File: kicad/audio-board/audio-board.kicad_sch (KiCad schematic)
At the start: 23 parts, among them U1 ADAU1861, U2 ADXL354CEZ, U3 LTC6242

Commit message: [LIMA] add IM72D128V PDM DMIC to the audio board - wired into U1's DMIC01/DMIC_CLK per docs/sensor-head-design-note.md S8
New Infineon.kicad_sym with the IM72D128V symbol (pinout from docs/datasheets/IM72D128V_v01_00.pdf
Table 9). Digital-only per the design note: no coupling, no buffer - straight into ADAU1861's
DMIC01/MP1 and DMIC_CLK/MP0. VDD on 1V8 (not 3V3, per JULIETT's 2026-09-17-004) with a 1uF bypass
cap at the VDD pad per the datasheet's footnote 3. LR tied to AGND (DATA1 channel) - my choice, not
specified anywhere, flagged in the schematic's open-items note for DSP-side confirmation. DMIC23/MP2
(the second mic pair) marked no-connect since this board carries one mic.
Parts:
- added C18: 1uF, symbol Device:C
- added U4: IM72D128VV01, symbol Infineon:IM72D128V
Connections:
- net 1V8: now also C18.1, U4.2 (VDD)
- net AGND: now also C18.2, U4.4 (LR), U4.5 (GND)
- net DMIC_DATA: now reaches U1.1 (DMIC01/MP1)
- net DMIC_DATA: now also U4.1 (DATA)
- net DMIC_CLK: now reaches U1.7 (DMIC_CLK/MP0)
- net DMIC_CLK: now also U4.3 (CLOCK)
- no-connect marks 13 -> 14
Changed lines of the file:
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@@
 		(at 72.39 86.36)
+	)
+	(no_connect
+		(at 234.95 142.24)
 	)
 	(wire
@@
 		)
 	)
-  (text "PRELIM - ADXL354 single-ended front end into the ADAU1861.\nPer docs/sensor-head-design-note.md and\ndocs/audio-board-decision-record.md (Decision B: ADAU1861\nruled, ADAU1372 rejected for this board).\n\nWIRED: ADAU1861 full power tree (1V8/AGND) + boot straps\n(PD, SELFBOOT, ROM_BOOT_MODE, REG_EN - tied to safe\ndefaults, [assumed], not checked against UG-2257's boot\nsection yet). ADXL354 X/Y/Z -> 100nF C0G coupling ->\n1Mohm bias to buffered CM -> LTC6242 unity-gain buffers\n-> AINN0/1/2, single-ended (AINP0/1/2 tied to raw CM).\n4th LTC6242 unit buffers CM per design note S6.\n\nNOT WIRED (deliberately, out of scope this pass):\ncontrol port (I2C/SPI), SAP0/SAP1 digital audio, JTAG,\nDMIC, UART, IRQ, QSPIM self-boot flash, headphone/line\noutputs, XTAL. ERC's 35 \"not connected\" errors are\nexactly these pins - expected, not a defect.\n\nOPEN ITEMS (design note S10 + new): buffer-to-AINNx\ncoupling (DC direct vs. footprint a series cap + 0R\njumper) not resolved here. CM pin loading not measured.\nSupply rail \"3V3_ACCEL\" is my judgment call, not in the\nnote - confirm before layout. REG_EN tied low assumes\nDVDD is externally supplied on 1V8, not the internal\nregulator - reasoned, not confirmed against the\ndatasheet's regulator sequencing section."
+	(label "1V8"
+		(at 177.8 121.92 0)
+		(effects
+			(font
+				(size 1.27 1.27)
+			)
+			(justify left bottom)
+		)
+	)
+	(label "AGND"
+		(at 177.8 129.54 0)
+		(effects
+			(font
+				(size 1.27 1.27)
+			)
+			(justify left bottom)
+		)
+	)
+	(label "DMIC_DATA"
+		(at 165.1 146.05 180)
+		(effects
+			(font
+				(size 1.27 1.27)
+			)
+			(justify right bottom)
+		)
+	)
+	(label "DMIC_CLK"
+		(at 190.5 146.05 0)
+		(effects
+			(font
+				(size 1.27 1.27)
+			)
+			(justify left bottom)
+		)
+	)
+	(label "AGND"
+		(at 190.5 148.59 0)
+		(effects
+			(font
+				(size 1.27 1.27)
+			)
+			(justify left bottom)
+		)
+	)
+	(label "1V8"
+		(at 177.8 160.02 0)
+		(effects
+			(font
+				(size 1.27 1.27)
+			)
+			(justify left bottom)
+		)
+	)
+	(label "AGND"
+		(at 177.8 134.62 0)
+		(effects
+			(font
+				(size 1.27 1.27)
+			)
+			(justify left bottom)
+		)
+	)
+	(label "DMIC_DATA"
+		(at 234.95 139.7 180)
+		(effects
+			(font
+				(size 1.27 1.27)
+			)
+			(justify right bottom)
+		)
+	)
+	(label "DMIC_CLK"
+		(at 234.95 144.78 180)
+		(effects
+			(font
+				(size 1.27 1.27)
+			)
+			(justify right bottom)
+		)
+	)
+  (text "PRELIM - ADXL354 single-ended front end into the ADAU1861.\nPer docs/sensor-head-design-note.md and\ndocs/audio-board-decision-record.md (Decision B: ADAU1861\nruled, ADAU1372 rejected for this board).\n\nWIRED: ADAU1861 full power tree (1V8/AGND) + boot straps\n(PD, SELFBOOT, ROM_BOOT_MODE, REG_EN - tied to safe\ndefaults, [assumed], not checked against UG-2257's boot\nsection yet). ADXL354 X/Y/Z -> 100nF C0G coupling ->\n1Mohm bias to buffered CM -> LTC6242 unity-gain buffers\n-> AINN0/1/2, single-ended (AINP0/1/2 tied to raw CM).\n4th LTC6242 unit buffers CM per design note S6.\nIM72D128V PDM mic -> DMIC01/DMIC_CLK on U1, per design\nnote S8 (digital-only, no coupling/buffer). VDD on 1V8\nwith 1uF bypass per datasheet footnote 3; LR tied to\nAGND (DATA1 channel). DMIC23/MP2 (2nd mic pair) marked\nno-connect - this board carries one mic.\n\nNOT WIRED (deliberately, out of scope this pass):\ncontrol port (I2C/SPI), SAP0/SAP1 digital audio, JTAG,\nUART, IRQ, QSPIM self-boot flash, headphone/line\noutputs, XTAL. ERC's \"not connected\" errors are exactly\nthese pins - expected, not a defect.\n\nOPEN ITEMS (design note S10 + new): buffer-to-AINNx\ncoupling (DC direct vs. footprint a series cap + 0R\njumper) not resolved here. CM pin loading not measured.\nSupply rail \"3V3_ACCEL\" is my judgment call, not in the\nnote - confirm before layout. REG_EN tied low assumes\nDVDD is externally supplied on 1V8, not the internal\nregulator - reasoned, not confirmed against the\ndatasheet's regulator sequencing section. DMIC LR=GND\n(DATA1) is my channel choice, not specified anywhere -\nconfirm against however the DSP expects the PDM stream\nframed."
     (at 100 215 0)
     (effects (font (size 1.2 1.2)))
@@
 					(unit 1)
 				)
+			)
+		)
+	)
+	(symbol
+		(lib_id "Infineon:IM72D128V")
+		(at 177.8 147.32 0)
+		(unit 1)
+		(in_bom yes)
+		(on_board yes)
+		(dnp no)
+		(property "Reference" "U4"
+			(at 177.8 134.62 0)
+			(effects
+				(font
+					(size 1.27 1.27)
+				)
+			)
+		)
+		(property "Value" "IM72D128VV01"
+			(at 177.8 160.02 0)
+			(effects
+				(font
+					(size 1.27 1.27)
+				)
+			)
+		)
+		(property "Footprint" ""
+			(at 177.8 147.32 0)
+			(hide yes)
+			(effects
+				(font
+					(size 1.27 1.27)
+				)
+			)
+		)
+		(property "Datasheet" "${KIPRJMOD}/../../docs/datasheets/IM72D128V_v01_00.pdf"
+			(at 177.8 147.32 0)
+			(hide yes)
+			(effects
+				(font
+					(size 1.27 1.27)
+				)
+			)
+		)
+		(instances
+			(project "audio-board"
+				(path "/58a3c587-b916-49c7-924f-a7f93d6c8ece"
+					(reference "U4")
+					(unit 1)
+				)
+			)
+		)
+	)
+	(symbol
+		(lib_id "Device:C")
+		(at 177.8 125.73 0)
+		(unit 1)
+		(in_bom yes)
+		(on_board yes)
+		(dnp no)
+		(property "Reference" "C18"
+			(at 178.435 123.19 0)
+			(effects
+				(font
+					(size 1.27 1.27)
+				)
+				(justify left)
+			)
+		)
+		(property "Value" "1uF"
+			(at 178.435 128.27 0)
+			(effects
+				(font
+					(size 1.27 1.27)
+				)
+				(justify left)
+			)
+		)
+		(property "Footprint" ""
+			(at 177.8 125.73 0)
+			(hide yes)
+			(effects
+				(font
+					(size 1.27 1.27)
+				)
+			)
+		)
+		(property "Datasheet" ""
+			(at 177.8 125.73 0)
+			(hide yes)
+			(effects
+				(font
+					(size 1.27 1.27)
+				)
+			)
+		)
+		(instances
+			(project "audio-board"
+				(path "/58a3c587-b916-49c7-924f-a7f93d6c8ece"
+					(reference "C18")
+					(unit 1)
+				)

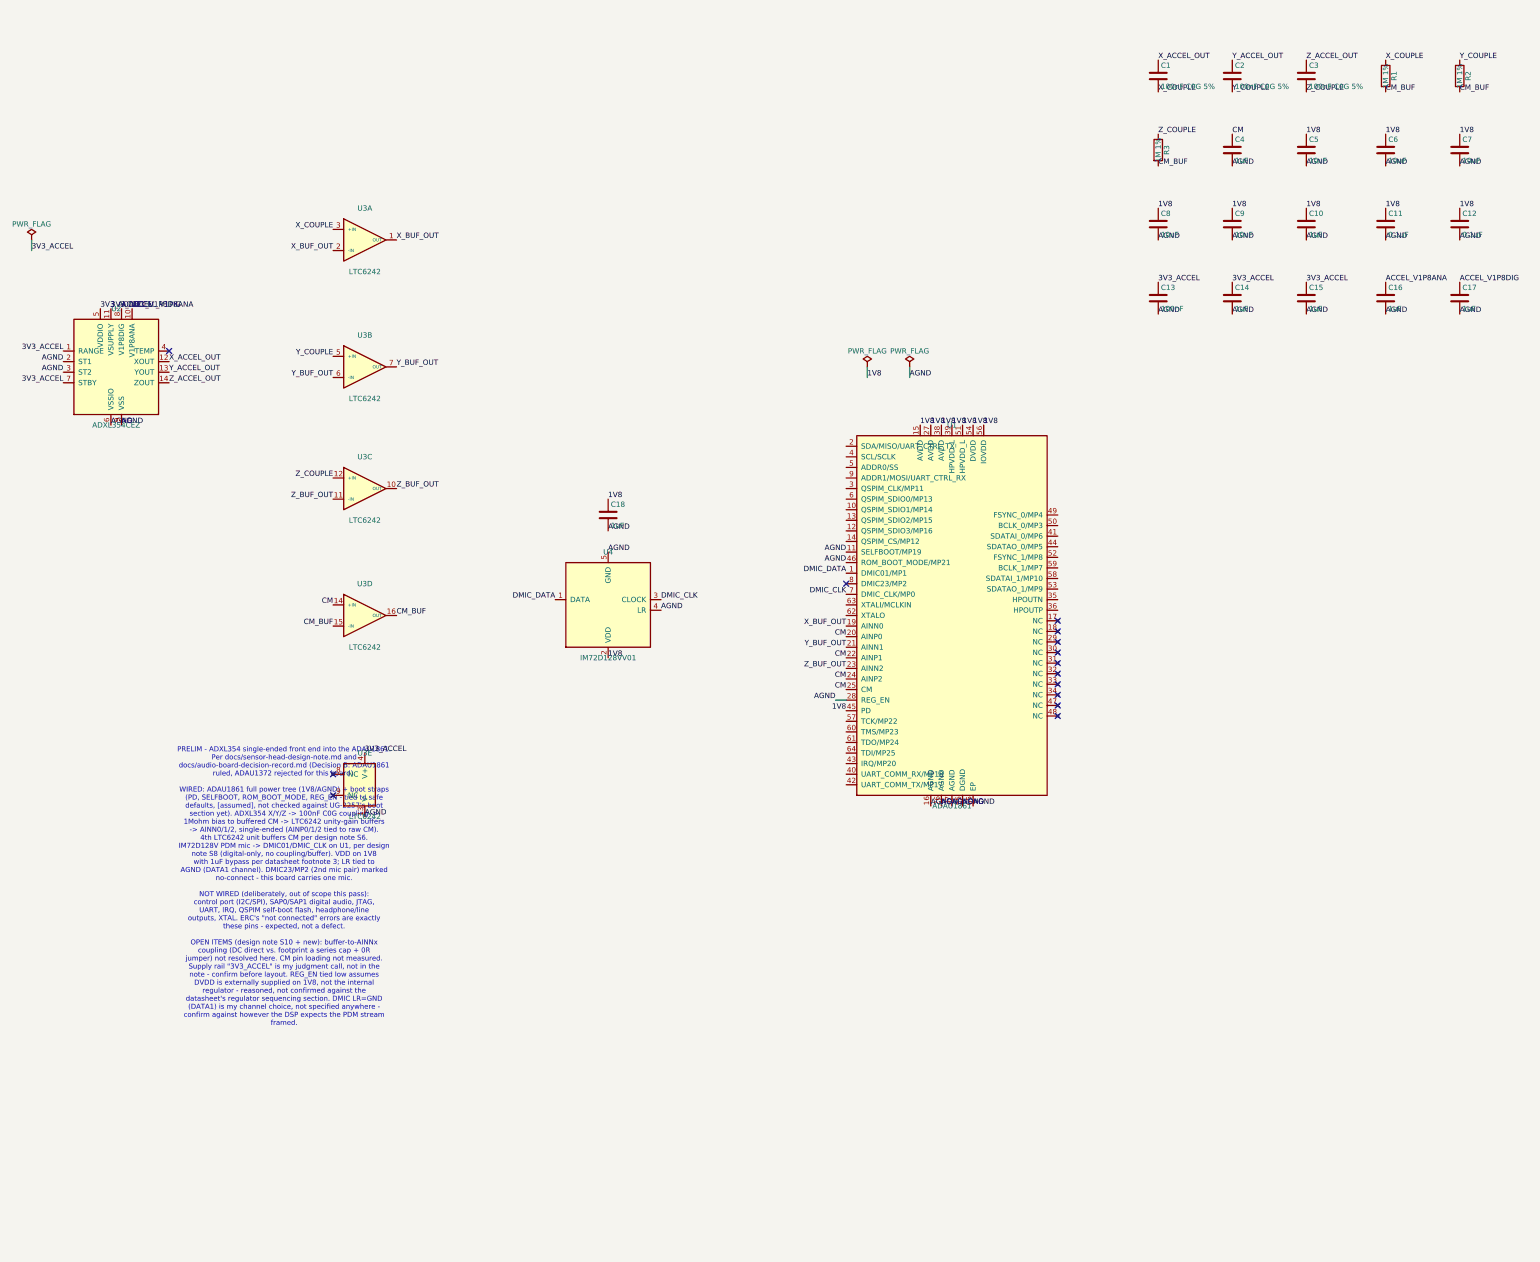
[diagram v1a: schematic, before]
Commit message: [LIMA] place AD2428 A2B transceiver on the audio board - host-side master node, for future connection to the earcups
New AD2428 symbol in AnalogDevices.kicad_sym (32-lead LFCSP_SS + EPAD, pinout from Table 15 of
docs/datasheets/AD242x_RevC.pdf). Per docs/audio-board-decision-record.md Decision C, this board's
AD2428 is the A2B bus MASTER: RP1 drives its I2S/TDM interface, and its Transceiver B pair runs
downstream to the per-cup slave transceivers.

Only wired what's unambiguous and chip-intrinsic: the on-chip LDO network (VOUT1 -> DVDD/PLLVDD,
VOUT2 -> ATRXVDD/BTRXVDD) with the datasheet's own decoupling values (4.7uF on each VOUTx, shared
100nF+10nF on the TRXVDD pins), and VSS/EPAD -> AGND (EPAD-to-GND is mandatory per the datasheet, not
a choice). Deliberately left open, flagged in the schematic's own note rather than guessed: VIN
(needs 3.7-9.0V, no such rail exists on this board yet), IOVDD's voltage domain (3.3V vs 1.8V,
decides whether U5 needs the same translators as the 1861), the entire host I2S/TDM + I2C interface,
the A2B bus-coupling network (the datasheet defers this to "contact your local ADI rep," which
docs/audio-board-decision-record.md's open item on the EVAL-AD2428WG1BZ already anticipated), and
whether the cups are bus-powered (decides SWP/VSSN/SENSE). ERC clean on everything wired; every new
"not connected" is one of these named opens.
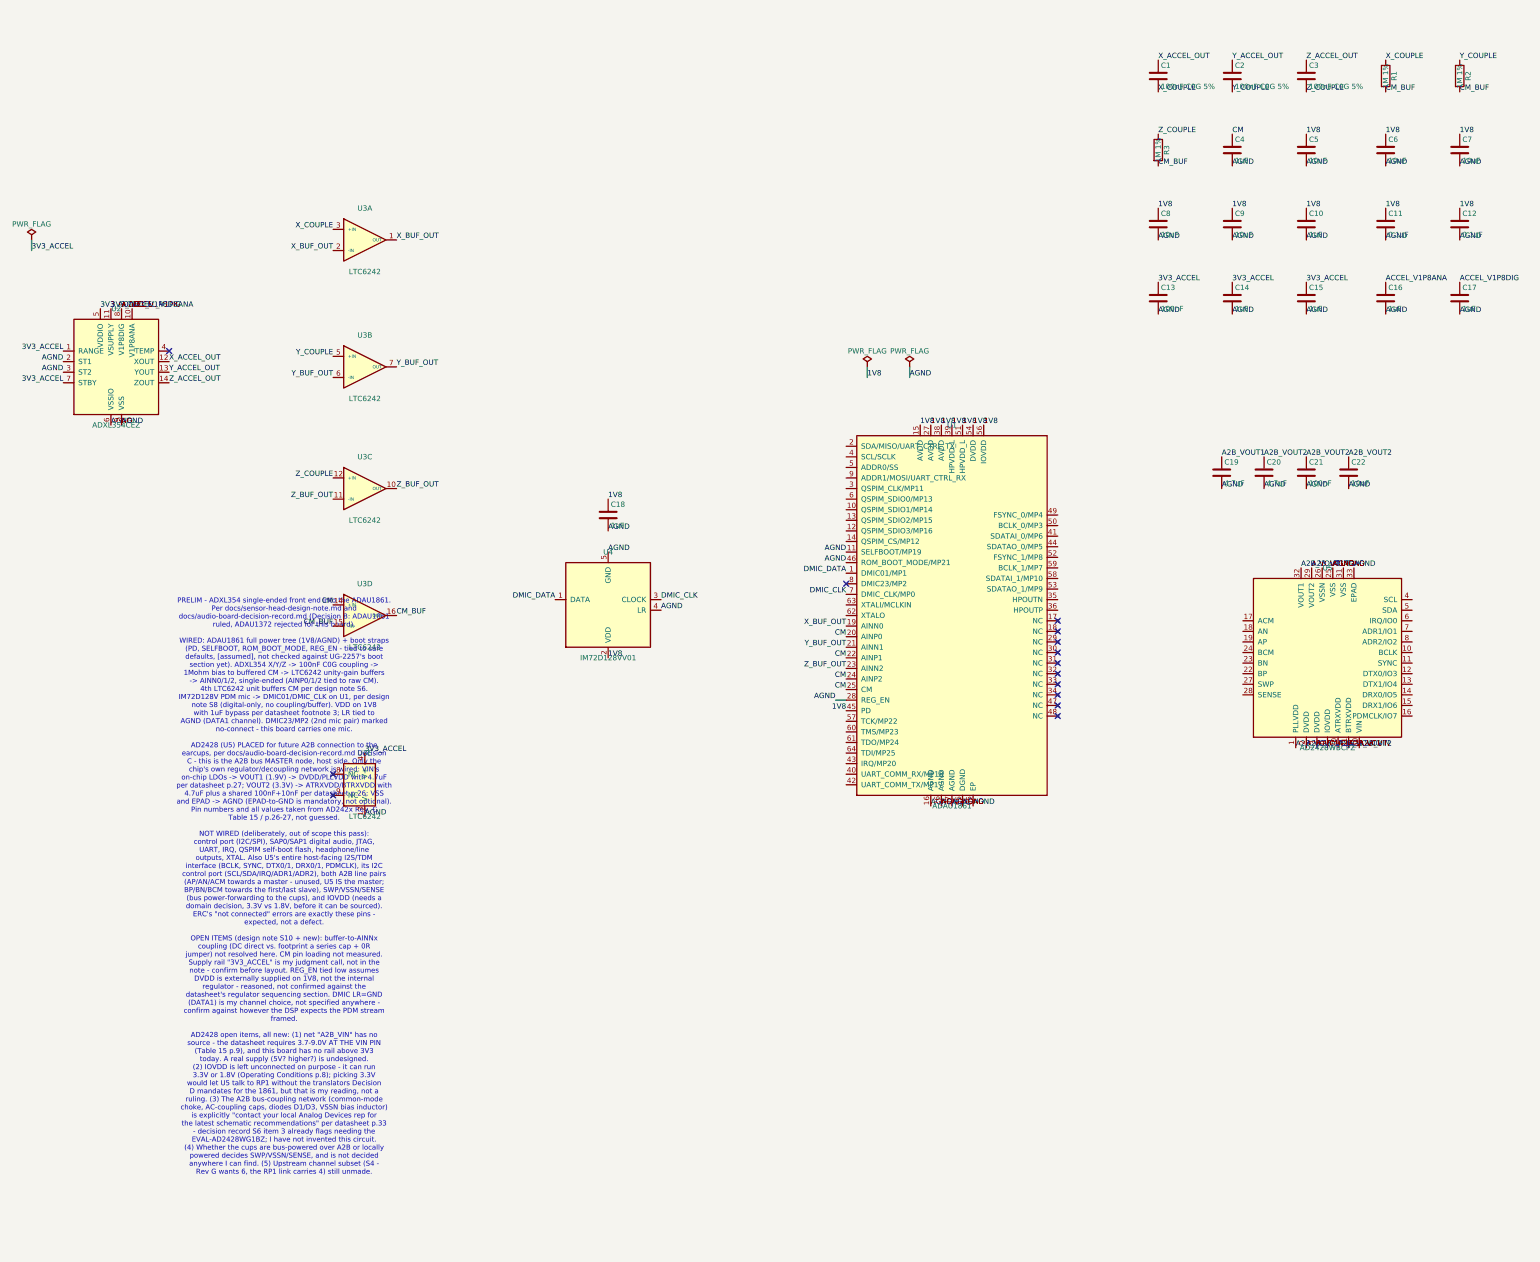
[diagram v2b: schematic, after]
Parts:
- added C19, C20: 4.7uF, symbol Device:C
- added C21: 100nF, symbol Device:C
- added C22: 10nF, symbol Device:C
- added U5: AD2428WBCPZ, symbol AnalogDevices:AD2428
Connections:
- net AGND: now also C19.2, C20.2, C21.2, C22.2, U5.25 (VSS), U5.31 (VSS), U5.33 (EPAD)
- new net A2B_VIN: U5.30 (VIN)
- new net A2B_VOUT1: C19.1, U5.1 (PLLVDD), U5.2 (DVDD), U5.3 (DVDD), U5.32 (VOUT1)
- new net A2B_VOUT2: C20.1, C21.1, C22.1, U5.20 (ATRXVDD), U5.21 (BTRXVDD), U5.29 (VOUT2)
